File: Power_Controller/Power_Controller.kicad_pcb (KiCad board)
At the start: 2 copper layers, 15 x 20 mm, 23 parts, among them J1 CONN_01X04_MALE, Q1 CSD16570Q5B, SW1 SW_Push, U1 MIC5060, U2 FAN4010, U3 STM32L021D4P6, U4 MPM3620A, U5 TCR2LE33LM

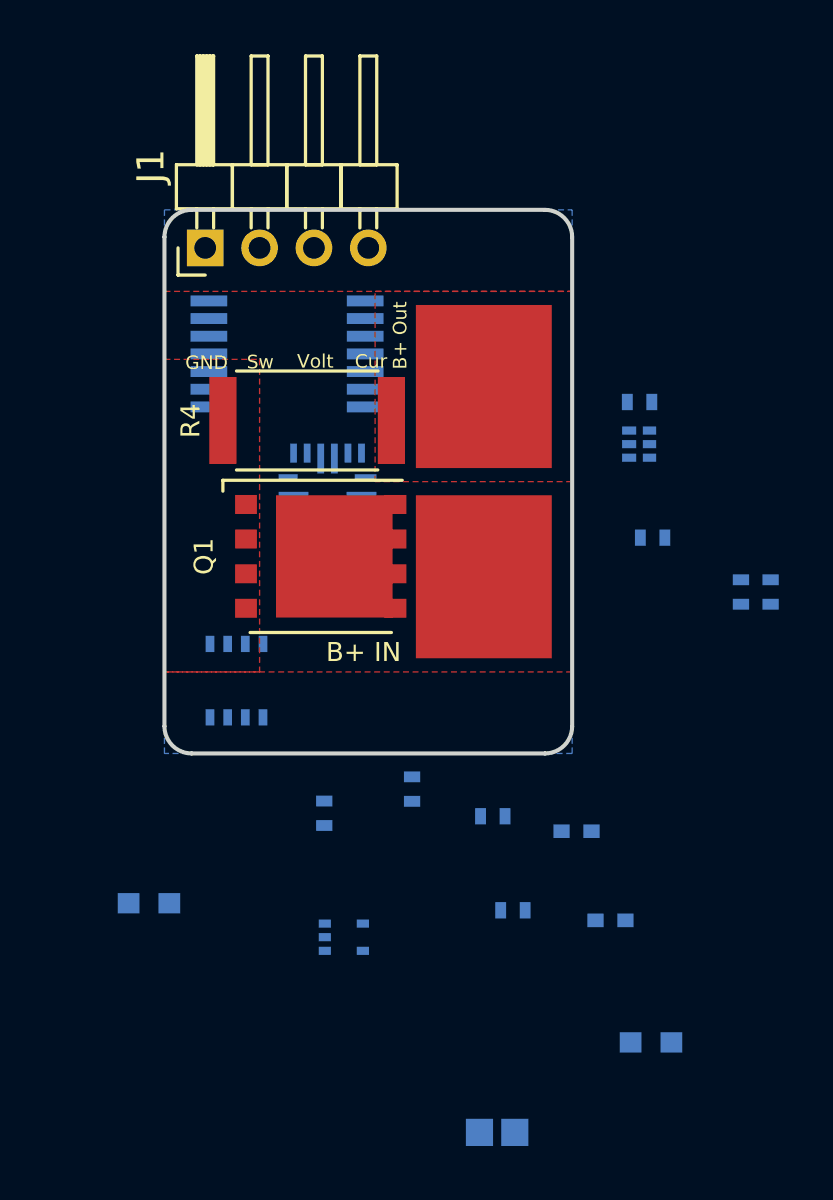
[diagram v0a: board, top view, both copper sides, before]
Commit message: V1.0 of the power controller, using the LTC2946
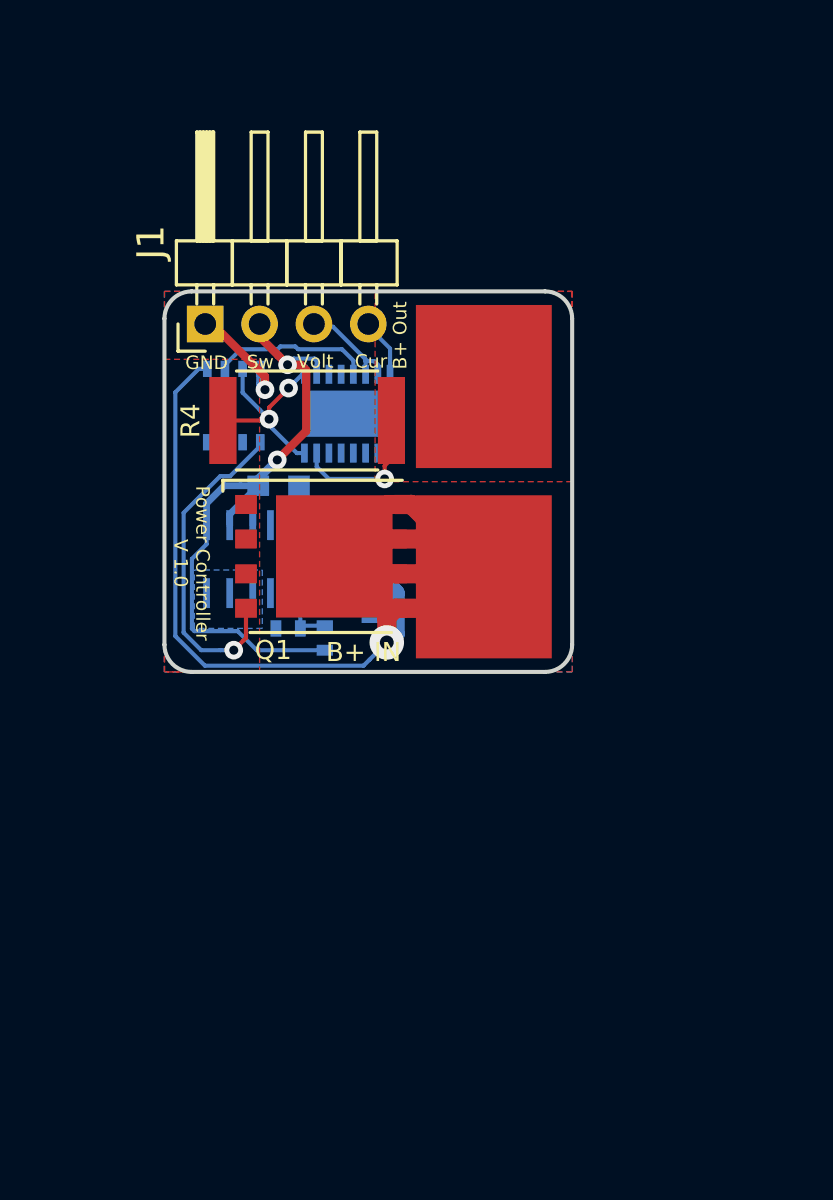
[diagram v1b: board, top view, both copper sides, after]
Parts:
- removed C3, C4: 100nF, Capacitors_SMD:C_0402
- removed R2: 2k, Resistors_SMD:R_0402
- removed R3, R6: 13k, Resistors_SMD:R_0402
- removed R5: 100R, Resistors_SMD:R_0402
- removed R9: 100k, Resistors_SMD:R_0402
- removed SW1: SW_Push, jumper:SOLDER-JUMPER_1-WAY
- removed U3: STM32L021D4P6, local:TSSOP14
- removed U5: TCR2LE33LM, TO_SOT_Packages_SMD:SOT-553
- R1: value 13k -> 200k
- U2: value FAN4010 -> LTC2946; footprint local:FAIRCHILD-MLP-6 -> local:LTC2946
- moved C2 24.6 mm to (146.7, 100.2)
- moved C1 15.5 mm to (149.9, 102.2), turned to 90 degrees
- moved R1 13.7 mm to (150.1, 104.5), turned to 90 degrees
- moved U2 10.8 mm to (149.2, 97.5), turned to 0 degrees
- moved R8 10.2 mm to (147.1, 105.4), turned to 180 degrees
- moved U1 10.1 mm to (145.1, 97.2)
- moved R7 6.42 mm to (148.4, 105.8), turned to 270 degrees
- moved J1 2.80 mm to (144.0, 94.2)
- moved U4 2.76 mm to (146.2, 102.8), turned to 180 degrees
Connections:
- J1 pad 3: USART2_RX -> I2C_SDA
- J1 pad 4: USART2_TX -> I2C_SCL
- Q1 pad 5: Net-(Q1-Pad5) -> +BATT
- R1 pad 1: VSENSE -> Net-(R1-Pad1)
- U1 pad 2: SWITCH -> Net-(U1-Pad2)
- U2 pad 2: (no net) -> +5V
- U2 pad 3: CSENSE -> (no net)
- U2 pad 5: GND -> Net-(U1-Pad2)
- U2 pad 6: Net-(R4-Pad2) -> I2C_SDA
- U4 pad 17: +BATT -> Net-(R1-Pad1)
- U4 pad 18: Net-(R9-Pad1) -> (no net)
- U4 pad 2: Net-(R9-Pad2) -> (no net)
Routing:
- net +BATT: track 0.00 -> 41.9 mm, vias 0 -> 1
- net +5V: track 0.00 -> 24.9 mm, vias 0 -> 2
- net Net-(Q1-Pad4): track 0.00 -> 12.2 mm, vias 0 -> 1
- net Net-(Q1-Pad1): track 0.00 -> 8.30 mm, vias 0 -> 2
- net Net-(U1-Pad2): track 0.00 -> 5.87 mm
- net Net-(R4-Pad2): track 0.00 -> 5.44 mm, vias 0 -> 1
- net GND: track 0.00 -> 4.32 mm, vias 0 -> 1
- net I2C_SDA: track 0.00 -> 3.84 mm
- net Net-(R1-Pad1): track 0.00 -> 2.35 mm
- net Net-(R7-Pad1): track 0.00 -> 2.17 mm
- net I2C_SCL: track 0.00 -> 2.08 mm
- added copper zone on B.Cu, net Net-(U4-Pad4)
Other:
- board size 15 x 20 mm -> 15 x 14 mm
- board text added: "Power Controller V 1.0"
- board text removed: "Power Switch V 1.0"

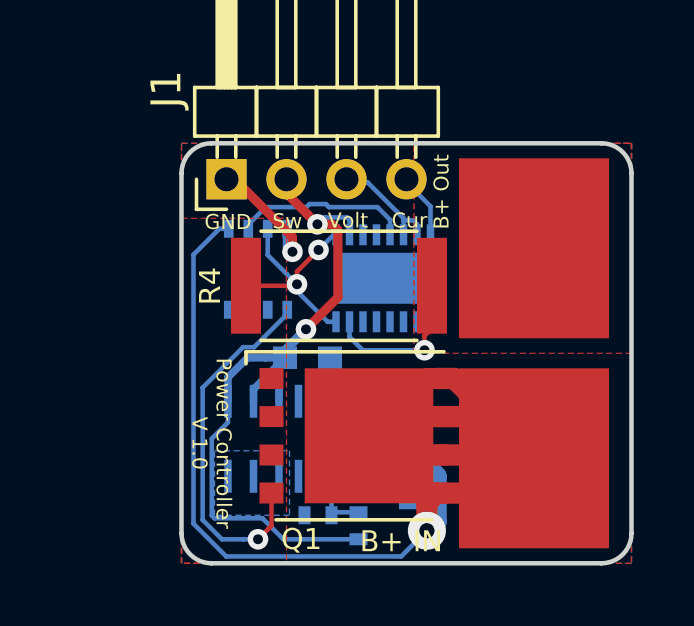
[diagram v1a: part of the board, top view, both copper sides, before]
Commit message: Updates GPS Diamond to 1.1.
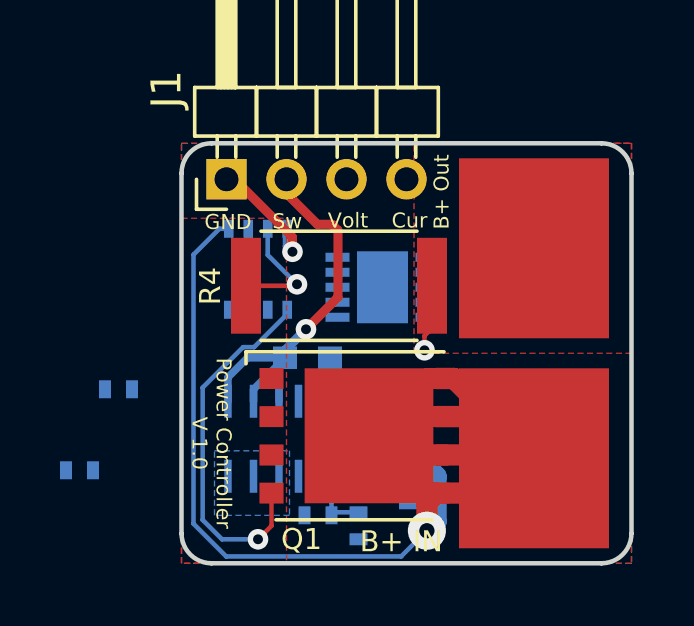
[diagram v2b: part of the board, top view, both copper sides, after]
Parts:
- added R2: 10k, Resistors_SMD:R_0402, B.Cu at (152.4, 96.0)
- added R3: 10k, Resistors_SMD:R_0402, B.Cu at (140.4, 101.2)
- added R5: 10k, Resistors_SMD:R_0402, B.Cu at (139.1, 103.9)
- U2: value LTC2946 -> PAC1710; footprint local:LTC2946 -> local:PAC1720
- moved U2 0.30 mm to (149.2, 97.8), turned to 90 degrees
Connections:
- R7 pad 1: Net-(R7-Pad1) -> +5V
- R7 pad 2: +5V -> Net-(R7-Pad2)
- R8 pad 1: Net-(R7-Pad1) -> Net-(R7-Pad2)
- U1 pad 2: Net-(U1-Pad2) -> Net-(R2-Pad1)
- U2 pad 10: (no net) -> +5V
- U2 pad 2: +5V -> Net-(R4-Pad2)
- U2 pad 3: (no net) -> GND
- U2 pad 4: (no net) -> GND
- U2 pad 5: Net-(U1-Pad2) -> GND
- U2 pad 6: I2C_SDA -> +5V
- U2 pad 7: I2C_SDA -> Net-(R2-Pad1)
- U2 pad 8: I2C_SCL -> I2C_SDA
- U2 pad 9: (no net) -> I2C_SCL
- U4 pad 1: Net-(R7-Pad1) -> Net-(R7-Pad2)
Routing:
- net +5V: track 24.9 -> 14.0 mm, vias 2 -> 1
- net Net-(U1-Pad2): track 5.87 -> 0.00 mm
- net Net-(Q1-Pad1): track 8.30 -> 4.11 mm, vias 2 -> 1
- net I2C_SDA: track 3.84 -> 0.00 mm
- net Net-(R4-Pad2): track 5.44 -> 2.25 mm
- net Net-(R7-Pad2): track 0.00 -> 2.17 mm
- net Net-(R7-Pad1): track 2.17 -> 0.00 mm
- net I2C_SCL: track 2.08 -> 0.00 mm
